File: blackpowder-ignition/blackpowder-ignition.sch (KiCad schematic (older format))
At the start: 7 parts, among them J1 CAS_stacking, J2 Conn_02x01, Q1 FDS6898A

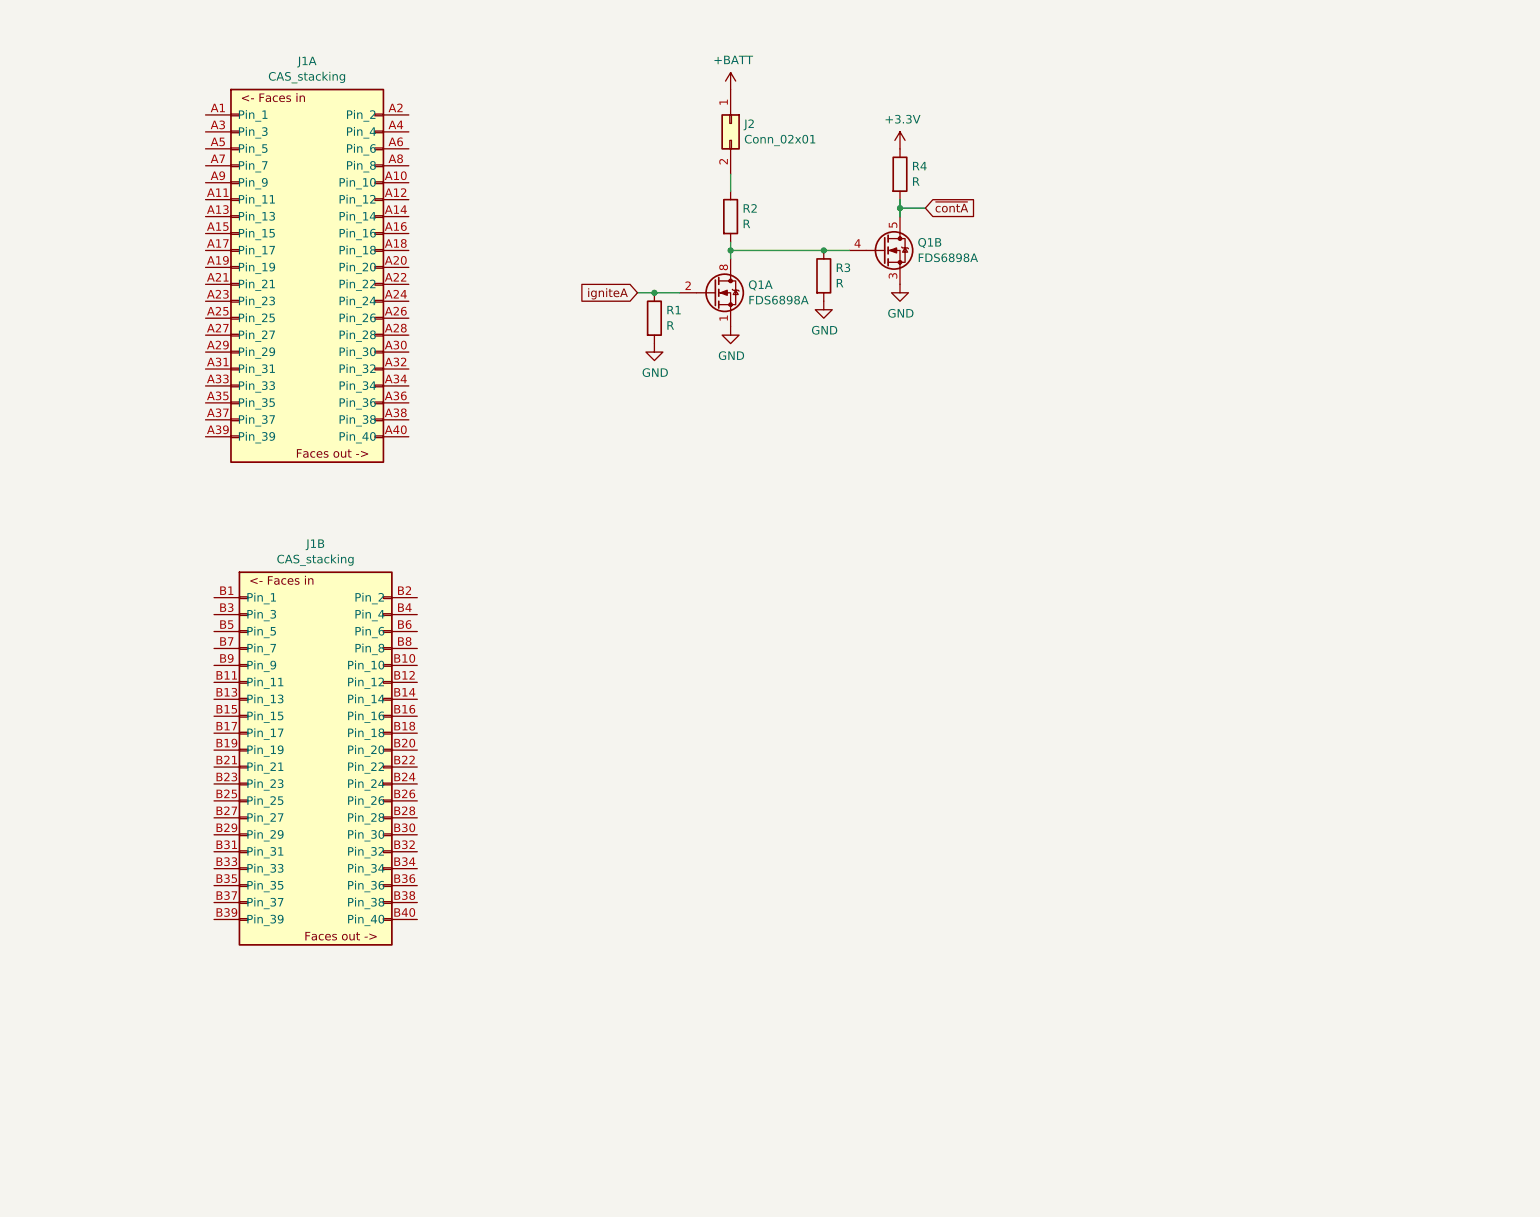
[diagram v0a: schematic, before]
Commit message: made hierarchical block for individual ignition circuit
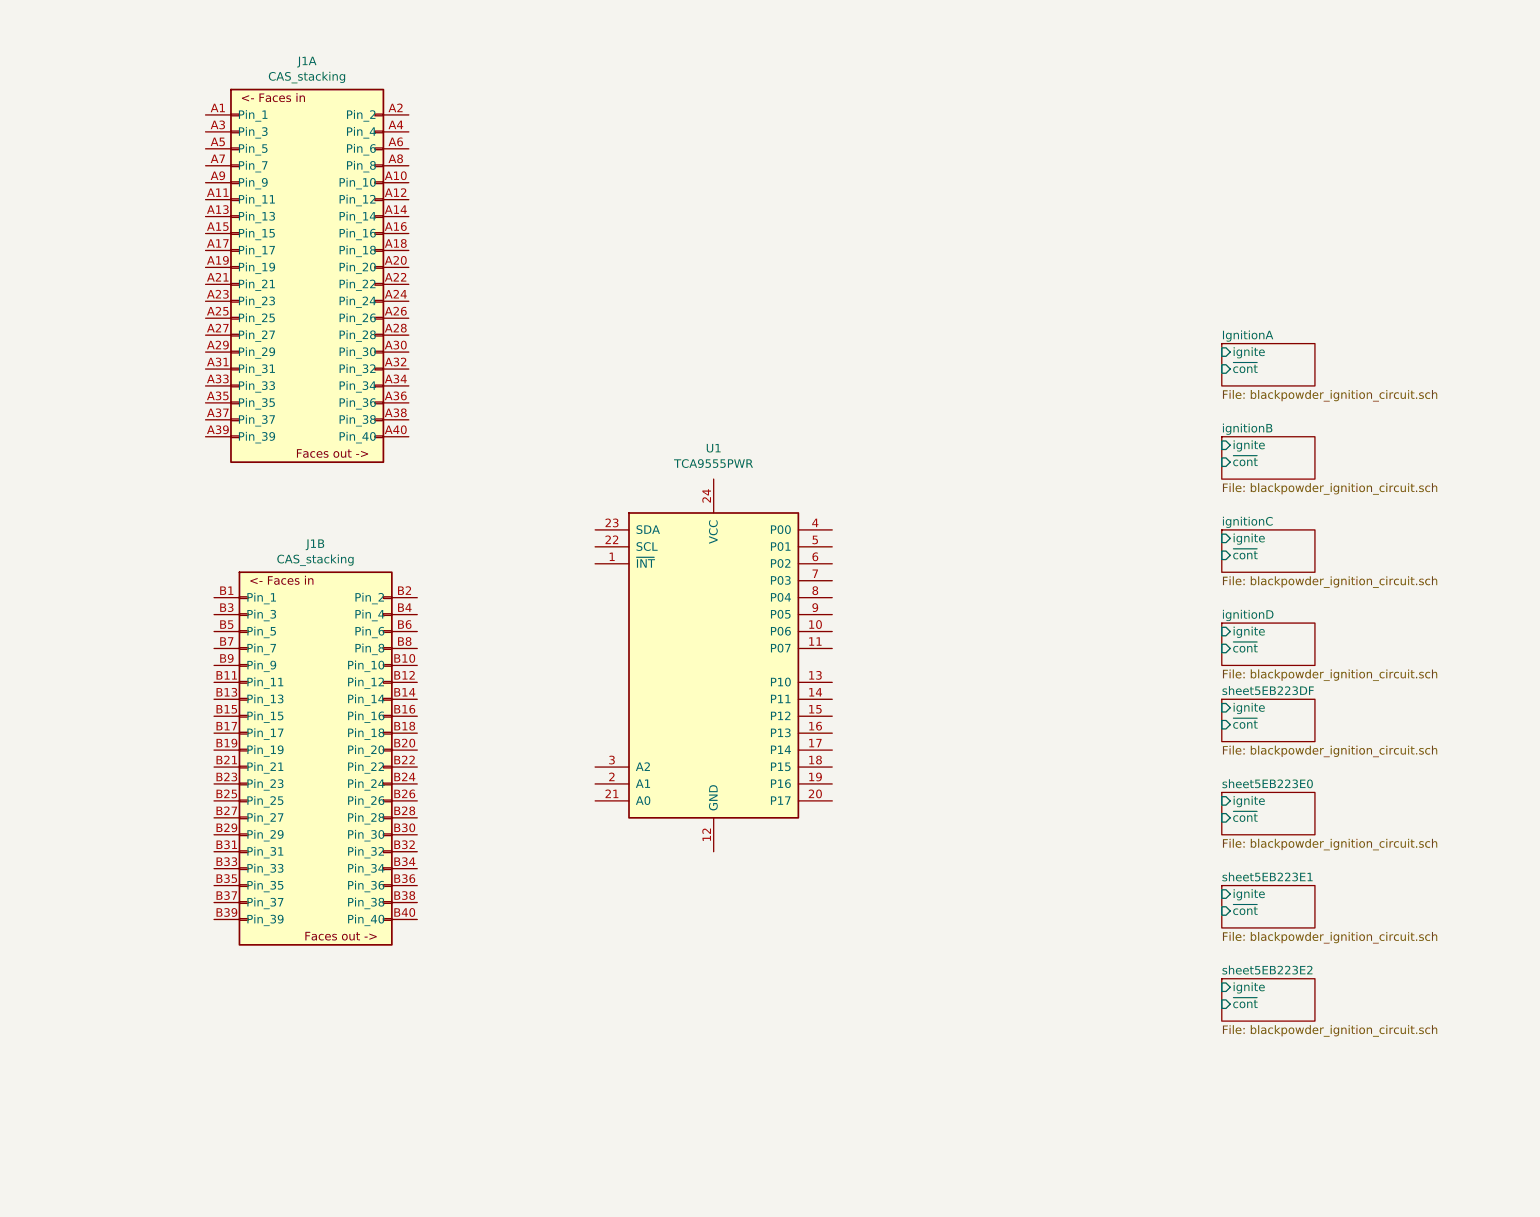
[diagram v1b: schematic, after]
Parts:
- removed J2: Conn_02x01, Connector_Molex:Molex_Mini-Fit_Jr_5569-02A2_2x01_P4.20mm_Horizontal, symbol Connector_Generic:Conn_02x01
- removed Q1: FDS6898A, Package_SO:SOIC-8_3.9x4.9mm_P1.27mm, symbol Transistor_FET:FDS6898A
- removed R1, R3, R4: R, Resistor_SMD:R_0603_1608Metric_Pad1.05x0.95mm_HandSolder, symbol Device:R
- removed R2: R, Package_TO_SOT_SMD:TO-252-3_TabPin2, symbol Device:R
- added U1: TCA9555PWR, Package_SO:TSSOP-24_4.4x7.8mm_P0.65mm, symbol Interface_Expansion:TCA9555PWR

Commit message: added hierarchical sch sheet for bus, address jummper pads, connections from io expander to subcircuits
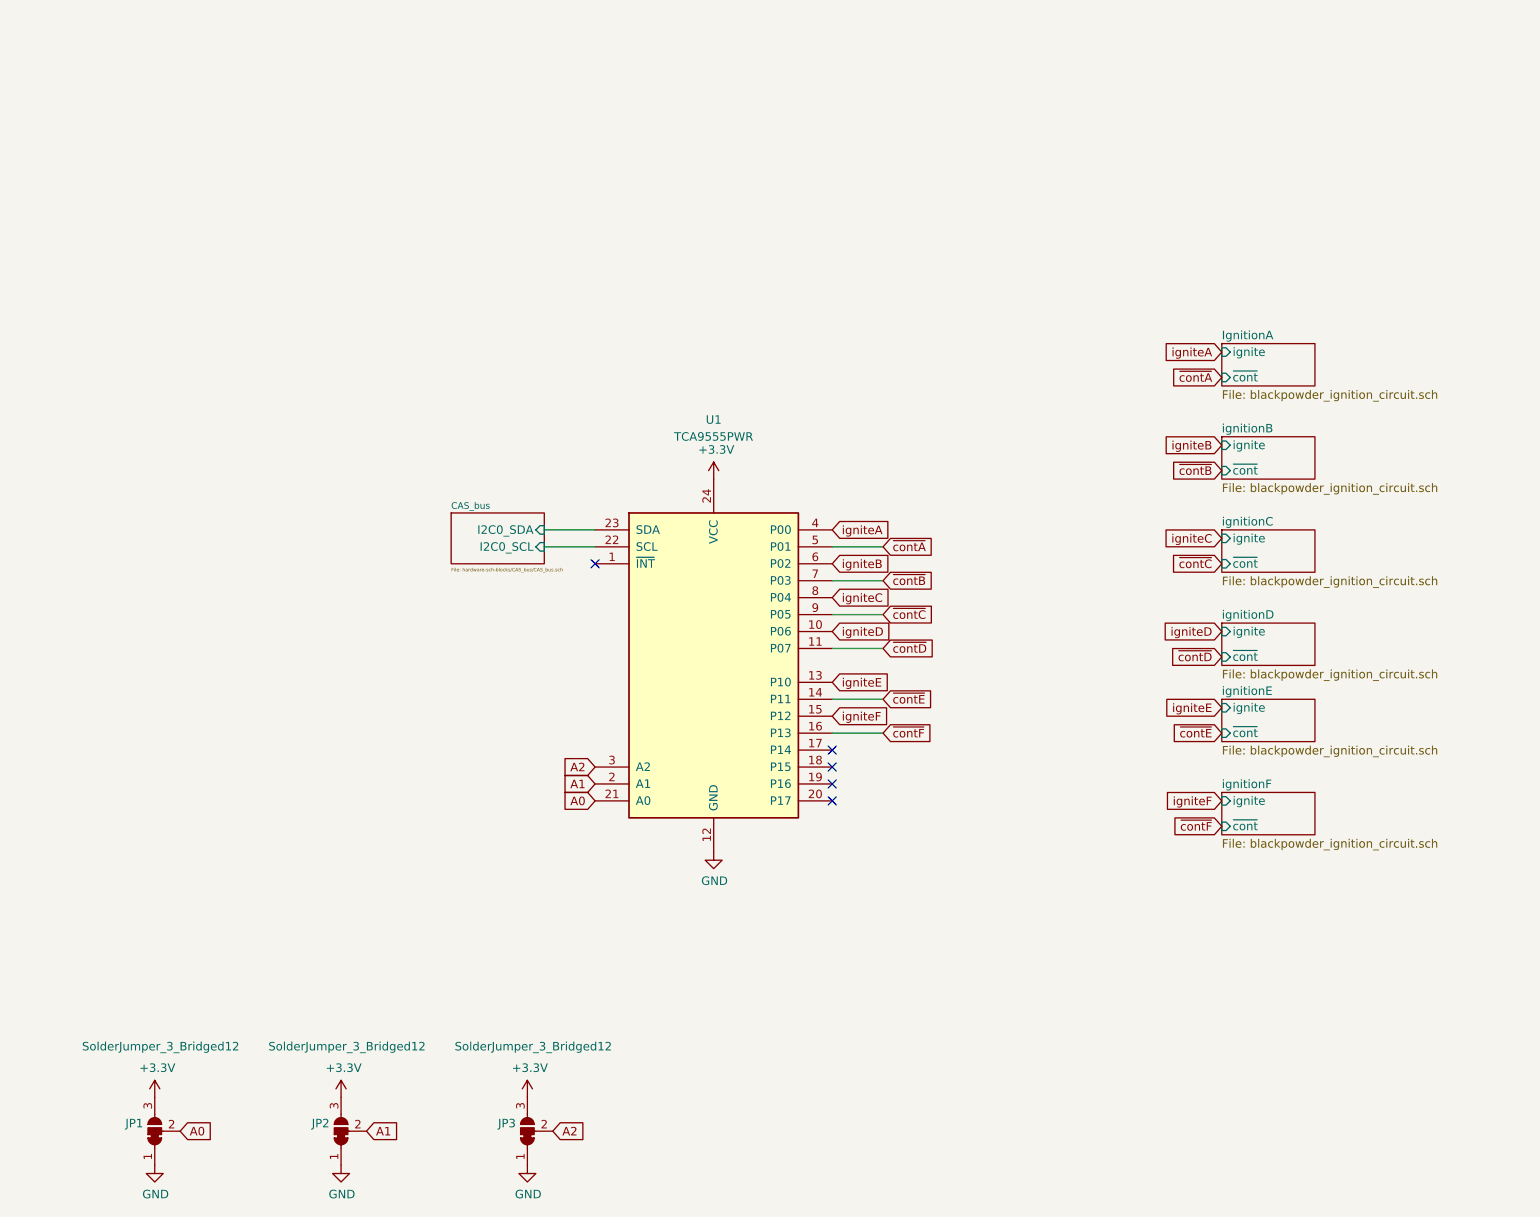
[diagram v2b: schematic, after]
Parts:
- removed J1: CAS_stacking, star-common-lib:CAS_physical, symbol star-common-lib:CAS_stacking
- added JP1, JP2, JP3: SolderJumper_3_Bridged12, Jumper:SolderJumper-3_P1.3mm_Bridged12_RoundedPad1.0x1.5mm, symbol Jumper:SolderJumper_3_Bridged12
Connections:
- net igniteD: now reaches U1.10 (P06)
- net ~contD~: now reaches U1.11 (P07)
- net GND: now reaches U1.12 (GND)
- net GND: now also JP1.1 (A), JP2.1 (A), JP3.1 (A)
- net igniteE: now reaches U1.13 (P10)
- net ~contE~: now reaches U1.14 (P11)
- net igniteF: now reaches U1.15 (P12)
- net ~contF~: now reaches U1.16 (P13)
- net A1: now reaches U1.2 (A1)
- net A1: now also JP2.2 (C)
- net A0: now reaches U1.21 (A0)
- net A0: now also JP1.2 (C)
- net CAS_bus/I2C0_SCL: now reaches U1.22 (SCL)
- net CAS_bus/I2C0_SDA: now reaches U1.23 (SDA)
- net +3V3: now reaches U1.24 (VCC)
- net +3V3: now also JP1.3 (B), JP2.3 (B), JP3.3 (B)
- net A2: now reaches U1.3 (A2)
- net A2: now also JP3.2 (C)
- net igniteA: now reaches U1.4 (P00)
- net ~contA~: now reaches U1.5 (P01)
- net igniteB: now reaches U1.6 (P02)
- net ~contB~: now reaches U1.7 (P03)
- net igniteC: now reaches U1.8 (P04)
- net ~contC~: now reaches U1.9 (P05)
- no-connect marks 0 -> 5

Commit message: added power connector
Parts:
- added J8: Conn_01x02, Connector_Molex:Molex_Mini-Fit_Jr_5569-02A2_2x01_P4.20mm_Horizontal, symbol Connector_Generic:Conn_01x02
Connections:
- net GND: now also J8.2 (Pin_2)
- new net +BATT: J8.1 (Pin_1)
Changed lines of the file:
@@
 Text GLabel 1400 7150 2    50   Input ~ 0
 A0
+$Comp
+L Connector_Generic:Conn_01x02 J8
+U 1 1 5ED34396
+P 1850 3750
+F 0 "J8" H 1930 3742 50  0000 L CNN
+F 1 "Conn_01x02" H 1930 3651 50  0000 L CNN
+F 2 "Connector_Molex:Molex_Mini-Fit_Jr_5569-02A2_2x01_P4.20mm_Horizontal" H 1850 3750 50  0001 C CNN
+F 3 "~" H 1850 3750 50  0001 C CNN
+	1    1850 3750
+	1    0    0    -1
+$EndComp
+$Comp
+L power:+BATT #PWR01
+U 1 1 5ED35440
+P 1650 3750
+F 0 "#PWR01" H 1650 3600 50  0001 C CNN
+F 1 "+BATT" H 1665 3923 50  0000 C CNN
+F 2 "" H 1650 3750 50  0001 C CNN
+F 3 "" H 1650 3750 50  0001 C CNN
+	1    1650 3750
+	1    0    0    -1
+$EndComp
+$Comp
+L power:GND #PWR02
+U 1 1 5ED356CF
+P 1650 3850
+F 0 "#PWR02" H 1650 3600 50  0001 C CNN
+F 1 "GND" H 1655 3677 50  0000 C CNN
+F 2 "" H 1650 3850 50  0001 C CNN
+F 3 "" H 1650 3850 50  0001 C CNN
+	1    1650 3850
+	1    0    0    -1
+$EndComp
 $EndSCHEMATC

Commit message: initial layout
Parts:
- added C1: 100nF, Capacitor_SMD:C_0603_1608Metric_Pad1.05x0.95mm_HandSolder, symbol Device:C
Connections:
- net +3V3: now also C1.1
- net GND: now also C1.2
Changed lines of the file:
@@
+	1    0    0    -1
+$EndComp
+$Comp
+L Device:C C1
+U 1 1 5EE696B1
+P 3400 4450
+F 0 "C1" H 3515 4496 50  0000 L CNN
+F 1 "100nF" H 3515 4405 50  0000 L CNN
+F 2 "Capacitor_SMD:C_0603_1608Metric_Pad1.05x0.95mm_HandSolder" H 3438 4300 50  0001 C CNN
+F 3 "~" H 3400 4450 50  0001 C CNN
+	1    3400 4450
+	1    0    0    -1
+$EndComp
+$Comp
+L power:+3.3V #PWR03
+U 1 1 5EE6DA21
+P 3400 4300
+F 0 "#PWR03" H 3400 4150 50  0001 C CNN
+F 1 "+3.3V" H 3415 4473 50  0000 C CNN
+F 2 "" H 3400 4300 50  0001 C CNN
+F 3 "" H 3400 4300 50  0001 C CNN
+	1    3400 4300
+	1    0    0    -1
+$EndComp
+$Comp
+L power:GND #PWR04
+U 1 1 5EE6DDF8
+P 3400 4600
+F 0 "#PWR04" H 3400 4350 50  0001 C CNN
+F 1 "GND" H 3405 4427 50  0000 C CNN
+F 2 "" H 3400 4600 50  0001 C CNN
+F 3 "" H 3400 4600 50  0001 C CNN
+	1    3400 4600
 	1    0    0    -1
 $EndComp

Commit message: nicer models, finished routing
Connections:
- net ~contF~ renamed ~igniteF~
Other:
- note added: "I/O Expander"
- note added: "I/O Expander Address Bits"
- note added: "Ignition Circuits"
- note added: "Power"
- moved on the sheet: C1, J8, JP1, JP2, JP3, U1
